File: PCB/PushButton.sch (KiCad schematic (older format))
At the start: 2 parts, among them SW2 PCB_Push_Button

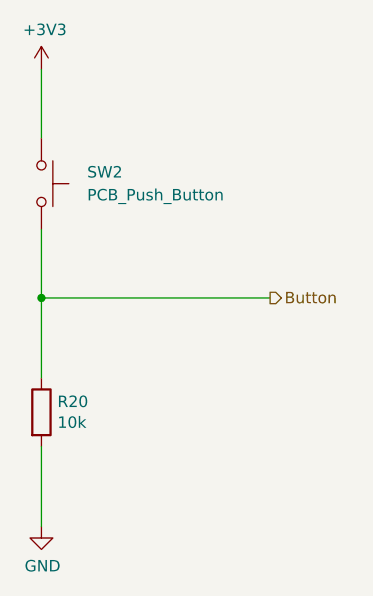
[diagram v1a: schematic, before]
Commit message: Improve the push buttons
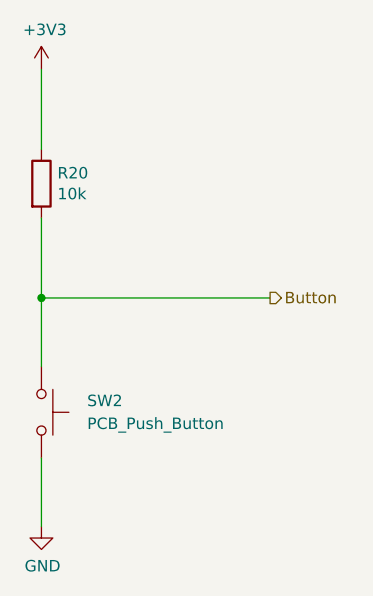
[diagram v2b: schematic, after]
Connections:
- net +3V3: now also R19.1; no longer SW2.1
- net Button: now also R19.2, SW2.1; no longer R19.1, SW2.2
- net GND: now also SW2.2; no longer R19.2
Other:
- moved on the sheet: R20, SW2
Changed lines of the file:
@@
 L Device:R R?
 U 1 1 604D6269
-P 5000 4000
+P 5000 3000
 AR Path="/603F20AB/604D6269" Ref="R?"  Part="1"
 AR Path="/603F1DCE/604D6269" Ref="R?"  Part="1"
@@
 AR Path="/603F1F4D/605BE11D/604D6269" Ref="R?"  Part="1"
 AR Path="/603F1F4D/605BE120/604D6269" Ref="R?"  Part="1"
-F 0 "R20" H 5070 4046 50  0000 L CNN
-F 1 "10k" H 5070 3955 50  0000 L CNN
-F 2 "Resistor_SMD:R_0603_1608Metric" V 4930 4000 50  0001 C CNN
-F 3 "https://www.bourns.com/docs/product-datasheets/CRxxxxx.pdf" H 5000 4000 50  0001 C CNN
-F 4 "CR0603-FX-1002ELF" H 5000 4000 50  0001 C CNN "Part_number"
-	1    5000 4000
+F 0 "R20" H 5070 3046 50  0000 L CNN
+F 1 "10k" H 5070 2955 50  0000 L CNN
+F 2 "Resistor_SMD:R_0603_1608Metric" V 4930 3000 50  0001 C CNN
+F 3 "https://www.bourns.com/docs/product-datasheets/CRxxxxx.pdf" H 5000 3000 50  0001 C CNN
+F 4 "CR0603-FX-1002ELF" H 5000 3000 50  0001 C CNN "Part_number"
+	1    5000 3000
 	1    0    0    -1
 $EndComp
@@
 $EndComp
 Wire Wire Line
-	5000 2500 5000 2800
-Wire Wire Line
-	5000 3200 5000 3500
-Wire Wire Line
-	5000 4150 5000 4500
-Wire Wire Line
 	6000 3500 5000 3500
 Connection ~ 5000 3500
 Wire Wire Line
-	5000 3500 5000 3850
+	5000 3500 5000 3800
 Text HLabel 6000 3500 2    50   Output ~ 0
 Button
@@
 L Switch:SW_Push SW2
 U 1 1 604CFE33
-P 5000 3000
+P 5000 4000
 AR Path="/603E03AA/603C09F0/604CFE33" Ref="SW2"  Part="1"
 AR Path="/603E03AA/603C05C6/604CFE33" Ref="SW?"  Part="1"
@@
 AR Path="/603F1F4D/605BE11D/604CFE33" Ref="SW?"  Part="1"
 AR Path="/603F1F4D/605BE120/604CFE33" Ref="SW?"  Part="1"
-F 0 "SW2" V 4950 3200 50  0000 L CNN
-F 1 "PCB_Push_Button" V 5050 3200 50  0000 L CNN
-F 2 "LitterRobot:PCB_Push_Button_5mm_0.4mm" H 5000 3200 50  0001 C CNN
-F 3 "~" H 5000 3200 50  0001 C CNN
-	1    5000 3000
+F 0 "SW2" V 4950 4200 50  0000 L CNN
+F 1 "PCB_Push_Button" V 5050 4200 50  0000 L CNN
+F 2 "LitterRobot:PCB_Push_Button_5mm_0.4mm" H 5000 4200 50  0001 C CNN
+F 3 "~" H 5000 4200 50  0001 C CNN
+	1    5000 4000
 	0    1    1    0
 $EndComp
+Wire Wire Line
+	5000 4200 5000 4500
+Wire Wire Line
+	5000 2500 5000 2850
+Wire Wire Line
+	5000 3150 5000 3500
 $EndSCHEMATC

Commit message: Add support for the weight sensor
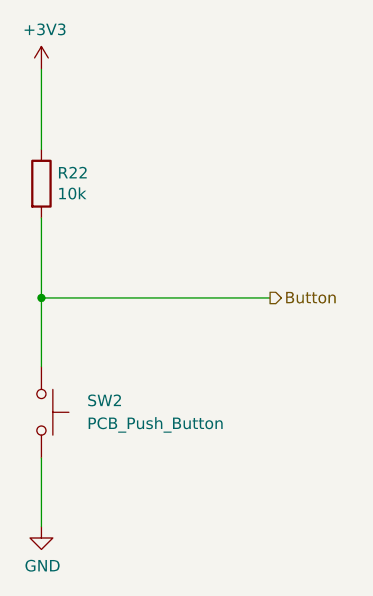
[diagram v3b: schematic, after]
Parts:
- renumbered R19 to R21
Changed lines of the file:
@@
 $Descr A4 11693 8268
 encoding utf-8
-Sheet 10 19
+Sheet 10 20
 Title "Litter Robot 3 - Push button (single)"
-Date "2021-03-28"
+Date "2021-04-02"
 Rev "A1"
 Comp "L. Sartory"
@@
 AR Path="/603F1DCE/604D6269" Ref="R?"  Part="1"
 AR Path="/603E03AA/603C05C6/604D6269" Ref="R?"  Part="1"
-AR Path="/603E03AA/603C0699/604D6269" Ref="R19"  Part="1"
+AR Path="/603E03AA/603C0699/604D6269" Ref="R21"  Part="1"
 AR Path="/603E03AA/603C06CF/604D6269" Ref="R?"  Part="1"
-AR Path="/603E03AA/603C09F0/604D6269" Ref="R20"  Part="1"
+AR Path="/603E03AA/603C09F0/604D6269" Ref="R22"  Part="1"
 AR Path="/603F1F4D/605BE11D/604D6269" Ref="R?"  Part="1"
 AR Path="/603F1F4D/605BE120/604D6269" Ref="R?"  Part="1"
-F 0 "R20" H 5070 3046 50  0000 L CNN
+F 0 "R22" H 5070 3046 50  0000 L CNN
 F 1 "10k" H 5070 2955 50  0000 L CNN
 F 2 "Resistor_SMD:R_0603_1608Metric" V 4930 3000 50  0001 C CNN
@@
 P 5000 2500
 AR Path="/603E03AA/603C05C6/604D6568" Ref="#PWR?"  Part="1"
-AR Path="/603E03AA/603C0699/604D6568" Ref="#PWR036"  Part="1"
+AR Path="/603E03AA/603C0699/604D6568" Ref="#PWR037"  Part="1"
 AR Path="/603E03AA/603C06CF/604D6568" Ref="#PWR?"  Part="1"
-AR Path="/603E03AA/603C09F0/604D6568" Ref="#PWR038"  Part="1"
+AR Path="/603E03AA/603C09F0/604D6568" Ref="#PWR039"  Part="1"
 AR Path="/603F1F4D/605BE11D/604D6568" Ref="#PWR?"  Part="1"
 AR Path="/603F1F4D/605BE120/604D6568" Ref="#PWR?"  Part="1"
-F 0 "#PWR038" H 5000 2350 50  0001 C CNN
+F 0 "#PWR039" H 5000 2350 50  0001 C CNN
 F 1 "+3V3" H 5015 2673 50  0000 C CNN
 F 2 "" H 5000 2500 50  0001 C CNN
@@
 P 5000 4500
 AR Path="/603E03AA/603C05C6/604D79CA" Ref="#PWR?"  Part="1"
-AR Path="/603E03AA/603C0699/604D79CA" Ref="#PWR037"  Part="1"
+AR Path="/603E03AA/603C0699/604D79CA" Ref="#PWR038"  Part="1"
 AR Path="/603E03AA/603C06CF/604D79CA" Ref="#PWR?"  Part="1"
-AR Path="/603E03AA/603C09F0/604D79CA" Ref="#PWR039"  Part="1"
+AR Path="/603E03AA/603C09F0/604D79CA" Ref="#PWR040"  Part="1"
 AR Path="/603F1F4D/605BE11D/604D79CA" Ref="#PWR?"  Part="1"
 AR Path="/603F1F4D/605BE120/604D79CA" Ref="#PWR?"  Part="1"
-F 0 "#PWR039" H 5000 4250 50  0001 C CNN
+F 0 "#PWR040" H 5000 4250 50  0001 C CNN
 F 1 "GND" H 5005 4327 50  0000 C CNN
 F 2 "" H 5000 4500 50  0001 C CNN

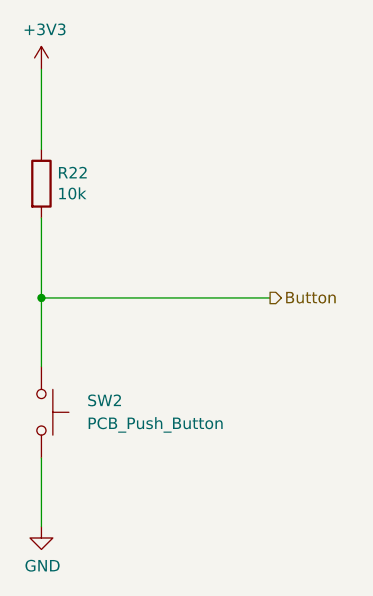
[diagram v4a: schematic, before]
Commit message: Re-annotate all components
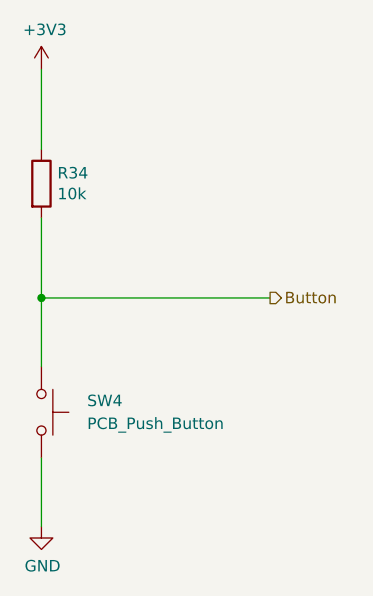
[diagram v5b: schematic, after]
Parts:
- renumbered R21 to R34, SW2 to SW1
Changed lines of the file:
@@
 $Descr A4 11693 8268
 encoding utf-8
-Sheet 10 22
+Sheet 14 22
 Title "Litter Robot 3 - Push button (single)"
-Date "2021-04-03"
+Date "2021-04-05"
 Rev "A1"
 Comp "L. Sartory"
@@
 AR Path="/603F1DCE/604D6269" Ref="R?"  Part="1"
 AR Path="/603E03AA/603C05C6/604D6269" Ref="R?"  Part="1"
-AR Path="/603E03AA/603C0699/604D6269" Ref="R21"  Part="1"
+AR Path="/603E03AA/603C0699/604D6269" Ref="R34"  Part="1"
 AR Path="/603E03AA/603C06CF/604D6269" Ref="R?"  Part="1"
-AR Path="/603E03AA/603C09F0/604D6269" Ref="R22"  Part="1"
+AR Path="/603E03AA/603C09F0/604D6269" Ref="R32"  Part="1"
 AR Path="/603F1F4D/605BE11D/604D6269" Ref="R?"  Part="1"
 AR Path="/603F1F4D/605BE120/604D6269" Ref="R?"  Part="1"
-F 0 "R22" H 5070 3046 50  0000 L CNN
+F 0 "R34" H 5070 3046 50  0000 L CNN
 F 1 "10k" H 5070 2955 50  0000 L CNN
 F 2 "Resistor_SMD:R_0603_1608Metric" V 4930 3000 50  0001 C CNN
@@
 P 5000 2500
 AR Path="/603E03AA/603C05C6/604D6568" Ref="#PWR?"  Part="1"
-AR Path="/603E03AA/603C0699/604D6568" Ref="#PWR037"  Part="1"
+AR Path="/603E03AA/603C0699/604D6568" Ref="#PWR088"  Part="1"
 AR Path="/603E03AA/603C06CF/604D6568" Ref="#PWR?"  Part="1"
-AR Path="/603E03AA/603C09F0/604D6568" Ref="#PWR039"  Part="1"
+AR Path="/603E03AA/603C09F0/604D6568" Ref="#PWR084"  Part="1"
 AR Path="/603F1F4D/605BE11D/604D6568" Ref="#PWR?"  Part="1"
 AR Path="/603F1F4D/605BE120/604D6568" Ref="#PWR?"  Part="1"
-F 0 "#PWR039" H 5000 2350 50  0001 C CNN
+F 0 "#PWR088" H 5000 2350 50  0001 C CNN
 F 1 "+3V3" H 5015 2673 50  0000 C CNN
 F 2 "" H 5000 2500 50  0001 C CNN
@@
 P 5000 4500
 AR Path="/603E03AA/603C05C6/604D79CA" Ref="#PWR?"  Part="1"
-AR Path="/603E03AA/603C0699/604D79CA" Ref="#PWR038"  Part="1"
+AR Path="/603E03AA/603C0699/604D79CA" Ref="#PWR089"  Part="1"
 AR Path="/603E03AA/603C06CF/604D79CA" Ref="#PWR?"  Part="1"
-AR Path="/603E03AA/603C09F0/604D79CA" Ref="#PWR040"  Part="1"
+AR Path="/603E03AA/603C09F0/604D79CA" Ref="#PWR085"  Part="1"
 AR Path="/603F1F4D/605BE11D/604D79CA" Ref="#PWR?"  Part="1"
 AR Path="/603F1F4D/605BE120/604D79CA" Ref="#PWR?"  Part="1"
-F 0 "#PWR040" H 5000 4250 50  0001 C CNN
+F 0 "#PWR089" H 5000 4250 50  0001 C CNN
 F 1 "GND" H 5005 4327 50  0000 C CNN
 F 2 "" H 5000 4500 50  0001 C CNN
@@
 Button
 $Comp
-L Switch:SW_Push SW2
+L Switch:SW_Push SW1
 U 1 1 604CFE33
 P 5000 4000
-AR Path="/603E03AA/603C09F0/604CFE33" Ref="SW2"  Part="1"
+AR Path="/603E03AA/603C09F0/604CFE33" Ref="SW1"  Part="1"
 AR Path="/603E03AA/603C05C6/604CFE33" Ref="SW?"  Part="1"
-AR Path="/603E03AA/603C0699/604CFE33" Ref="SW1"  Part="1"
+AR Path="/603E03AA/603C0699/604CFE33" Ref="SW4"  Part="1"
 AR Path="/603E03AA/603C06CF/604CFE33" Ref="SW?"  Part="1"
 AR Path="/603F1F4D/605BE11D/604CFE33" Ref="SW?"  Part="1"
 AR Path="/603F1F4D/605BE120/604CFE33" Ref="SW?"  Part="1"
-F 0 "SW2" V 4950 4200 50  0000 L CNN
+F 0 "SW4" V 4950 4200 50  0000 L CNN
 F 1 "PCB_Push_Button" V 5050 4200 50  0000 L CNN
 F 2 "LitterRobot:PCB_Push_Button_5mm_0.4mm" H 5000 4200 50  0001 C CNN

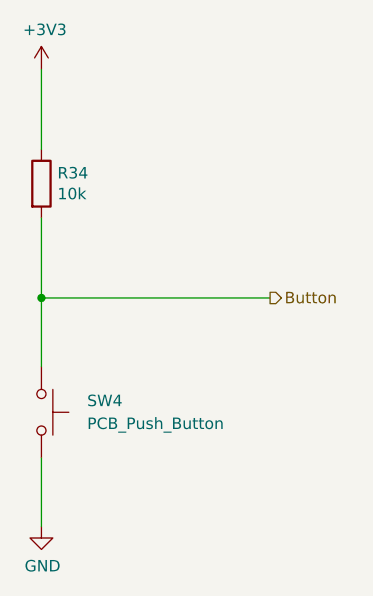
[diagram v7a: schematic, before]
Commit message: Add jumpers on the power supply outputs
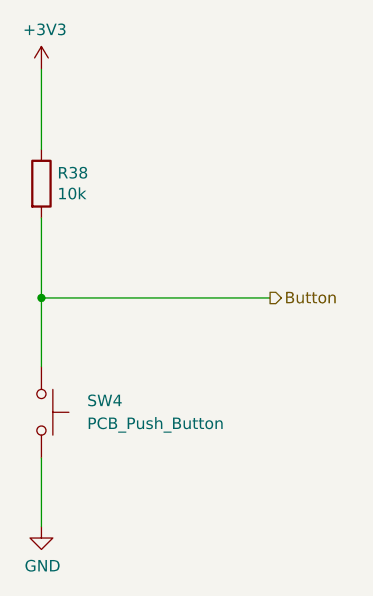
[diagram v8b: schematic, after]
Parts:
- renumbered R34 to R38
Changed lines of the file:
@@
 Sheet 15 23
 Title "Litter Robot 3 - Push button (single)"
-Date "2021-04-10"
+Date "2021-05-24"
 Rev "A1"
 Comp "L. Sartory"
@@
 AR Path="/603F1DCE/604D6269" Ref="R?"  Part="1"
 AR Path="/603E03AA/603C05C6/604D6269" Ref="R?"  Part="1"
-AR Path="/603E03AA/603C0699/604D6269" Ref="R34"  Part="1"
+AR Path="/603E03AA/603C0699/604D6269" Ref="R38"  Part="1"
 AR Path="/603E03AA/603C06CF/604D6269" Ref="R?"  Part="1"
-AR Path="/603E03AA/603C09F0/604D6269" Ref="R32"  Part="1"
+AR Path="/603E03AA/603C09F0/604D6269" Ref="R36"  Part="1"
 AR Path="/603F1F4D/605BE11D/604D6269" Ref="R?"  Part="1"
 AR Path="/603F1F4D/605BE120/604D6269" Ref="R?"  Part="1"
-F 0 "R34" H 5070 3046 50  0000 L CNN
+F 0 "R38" H 5070 3046 50  0000 L CNN
 F 1 "10k" H 5070 2955 50  0000 L CNN
 F 2 "Resistor_SMD:R_0603_1608Metric" V 4930 3000 50  0001 C CNN
